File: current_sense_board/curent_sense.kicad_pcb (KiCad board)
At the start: 2 copper layers, 50.4 x 63 mm, 19 parts, among them J1 Screw_Terminal_01x01, J10 Conn_01x05_Pin, J2 Screw_Terminal_01x01, J3 Screw_Terminal_01x01, J4 Screw_Terminal_01x01, J7 Screw_Terminal_01x01, J8 Screw_Terminal_01x01, U1 ACS758KCB-150B-PFF-T, U2 ACS758KCB-150B-PFF-T, U8 ACS758KCB-150B-PFF-T

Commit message: did stuff
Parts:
- added D1: LED, LED_SMD:LED_0603_1608Metric_Pad1.05x0.95mm_HandSolder, F.Cu at (82.1, 74.4)
- added R5: 330, Resistor_SMD:R_0603_1608Metric_Pad0.98x0.95mm_HandSolder, F.Cu at (82.1, 76.2)
- moved U1 11.7 mm to (68.3, 112.1)
- moved J1 11.7 mm to (49.4, 116.6)
- moved J2 11.7 mm to (49.4, 107.2)
- moved C1 11.7 mm to (81.8, 112.9)
- moved R1 11.7 mm to (82.8, 110.1)
- moved R2 11.7 mm to (85.4, 111.1)
- moved U2 5.49 mm to (68.3, 85.3)
- moved C2 5.49 mm to (81.8, 86.3)
- moved J3 5.49 mm to (49.2, 90.5)
- moved J4 5.49 mm to (49.2, 80.7)
- moved R3 5.49 mm to (82.7, 83.5)
- moved R4 5.49 mm to (85.4, 84.5)
- moved J7 0.60 mm to (49.4, 63.8)
- moved C38 0.60 mm to (81.7, 59.7)
- moved J8 0.60 mm to (49.4, 53.9)
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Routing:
- net +5V: track 66.0 -> 138.0 mm
- net /ADC2: track 16.7 -> 28.4 mm
- net /ADC1: track 9.80 -> 6.70 mm
- net Net-(D1-K): track 0.00 -> 1.80 mm
- net /ADC0: track 26.7 -> 28.3 mm
- net GND: track 0.00 -> 0.54 mm
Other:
- board size 50.4 x 63 mm -> 50.4 x 74.2 mm

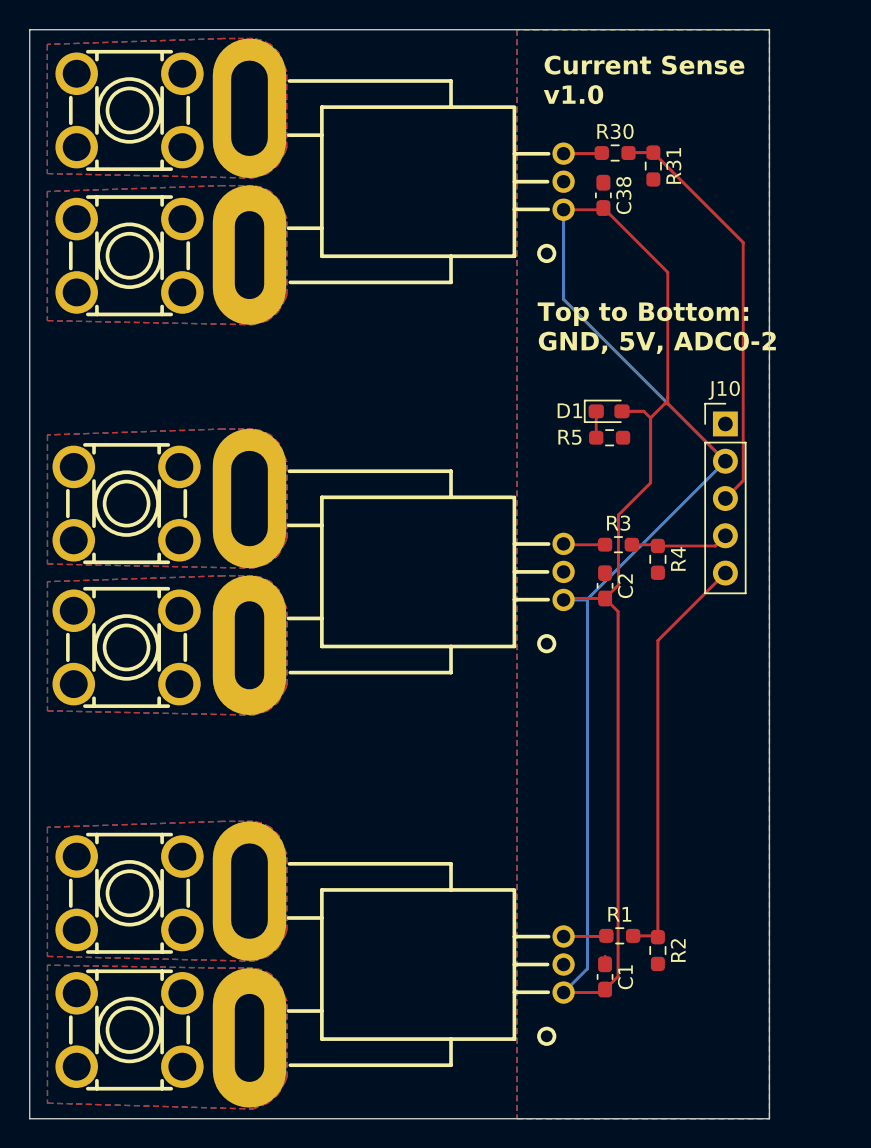
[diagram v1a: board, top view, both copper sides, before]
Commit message: mounting holes
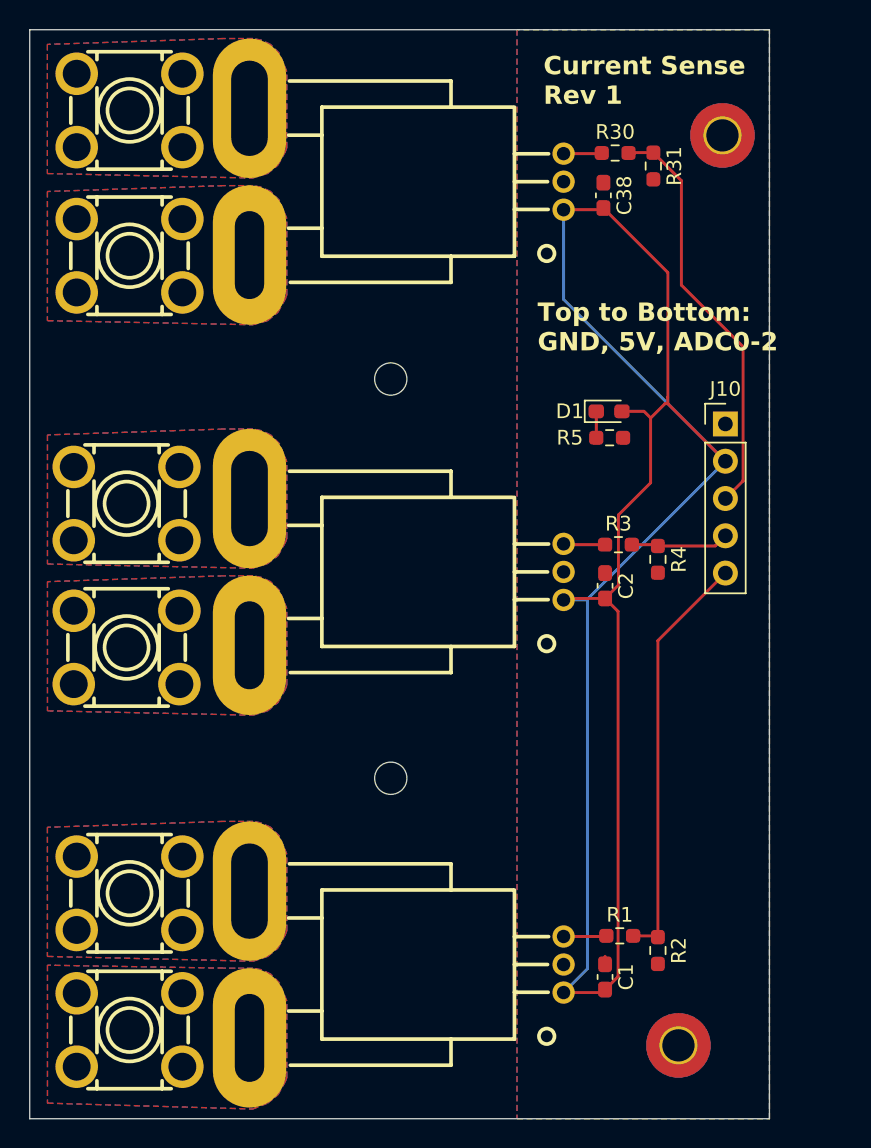
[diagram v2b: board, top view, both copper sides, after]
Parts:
- added H1: MountingHole, MountingHole:MountingHole_2.2mm_M2, F.Cu at (67.2, 72.2)
- added H2: MountingHole, MountingHole:MountingHole_2.2mm_M2, F.Cu at (67.2, 99.4)
- added H3: MountingHole_Pad, MountingHole:MountingHole_2.2mm_M2_Pad_TopBottom, F.Cu at (89.8, 55.6)
- added H5: MountingHole_Pad, MountingHole:MountingHole_2.2mm_M2_Pad_TopBottom, F.Cu at (86.8, 117.6)
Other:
- board text added: "Current Sense Rev 1"
- board text removed: "Current Sense v1.0"
